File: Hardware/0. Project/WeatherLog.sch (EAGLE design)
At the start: 40 parts, among them IC2 TP4056, IC3 DS3231/SO, IC4 DW01A-G, U2 FS8205A, U3 ATMEGA328P-AU, U4 RT9193-33GB

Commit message: Working on 1.0 schematic
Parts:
- removed D3: SS16, diode:SUPPRESSOR-SMBJ
- removed LED1, LED2: (no value), led:LEDCHIPLED_0805
- removed LED3: IN-PI556FCH, LED RGB SMD:IN-PI556FCH
- removed R13: 150R (5%), rcl:R-EU_R0603
- removed R14, R17: 50R (5%), rcl:R-EU_R0603
- added C1, C2: 1uF, rcl:C-EUC0805
- added LED6: RGBLED5050, adafruit:RGBLED5050
- added Q1: BC817, transistor-npn:BC817-40LT1SMD
- added R1: 10k, rcl:R-EU_R0603
- added R12: NC, rcl:R-EU_R0603
- added R2: 20R, rcl:R-EU_R0603
- added R8, R9: 1k, rcl:R-EU_R0603
- added U1: ESP8266EX, ESP8266EX:ESP8266EX
- added U5: 25Q80ASSIG, 25Q80ASSIG:25Q80ASSIG
- R6: value 1k -> 100k
- R7: value 1k -> 200R
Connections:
- removed net +5V: U4.VOUT
- removed net BAT_CHARGING: IC2.!CHRG, LED1.C, U3.PD0
- removed net BAT_STANDBY: IC2.!STDBY, LED2.C, U3.PD1
- removed net N$26: LED3.AB3, R17.2
- removed net V_BAT: BT1.+, C5.1, IC2.BAT, R20.1, R4.1, U4.EN, U4.VIN
- removed net V_POWER_SUPPLY: C4.1, D3.A, IC2.CE, IC2.VCC4, J1.3, R18.1, R6.2, R7.2
- new net !BAT_CHARGING!: IC2.!CHRG, LED6.GREEN_C, U3.PD0
- new net !BAT_STANDBY!: IC2.!STDBY, LED6.BLUE_C, U3.PD1
- new net N$1: Q1.B, R1.1
- new net N$12: LED6.BLUE_A, R9.1
- new net N$13: R7.1, U5.SCLK
- new net N$15: U1.SDIO_DATA_0, U5.MOSI
- new net N$23: R7.2, U1.SDIO_CLK
- new net N$24: R12.1, U1.!EXT_RSTB
- new net N$25: R12.2, U1.XPD_DCDC
- new net N$3: LED6.RED_C, Q1.C
- new net N$5: LED6.RED_A, R2.1
- new net V_BAT+: BT1.+, C2.1, C5.1, IC2.BAT, R2.2, R20.1, R4.1, R6.2, U4.EN, U4.VIN
- new net V_BAT-: BT1.-, C3.2, IC4.GND, Q1.E, U2.S1_1
- new net V_EXTERNAL_SUPPLY: C1.1, C4.1, IC2.CE, IC2.VCC4, J1.3, R18.1, R8.2, R9.2, U4.VOUT
- net 3V: no longer D3.C
- net BAT_OVER_DISCHARGE_DETECTED: now also R1.2
- net GND: now also C1.2, C2.2, R6.1; no longer LED3.KB4, LED3.KG6, LED3.KR5
- net LED_BLUE: no longer R17.1
- net LED_GREEN: no longer R14.1
- net LED_RED: no longer R13.1
- net N$10: now also LED6.GREEN_A, R8.1; no longer BT1.-, C3.2, IC4.GND, U2.S1_1
- net N$11: now also U1.SDIO_DATA_3, U5.!WP!; no longer LED1.A, R6.1
- net N$14: now also U1.SDIO_DATA_2, U5.!HOLD!; no longer LED2.A, R7.1
- net N$2: now also U1.SDIO_CMD, U5.!CS!; no longer LED3.AR2, R13.2
- net N$21: now also U1.SDIO_DATA_1, U5.MISO; no longer LED3.AG1, R14.2
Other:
- note added: "BATTERY STATUS"
- note added: "RECHARGEABLE BATTERY"
- note removed: "(Over-Charge & Over-Discharge)"
- note removed: "(outdoor WeatherLog Mode)"
- note removed: "LI-PO BATTERY"
- note removed: "USER INTERFACE"
- moved on the sheet: BT1, C3, C4, C5, C9, IC2, IC3, IC4, J1, R10, R11, R3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

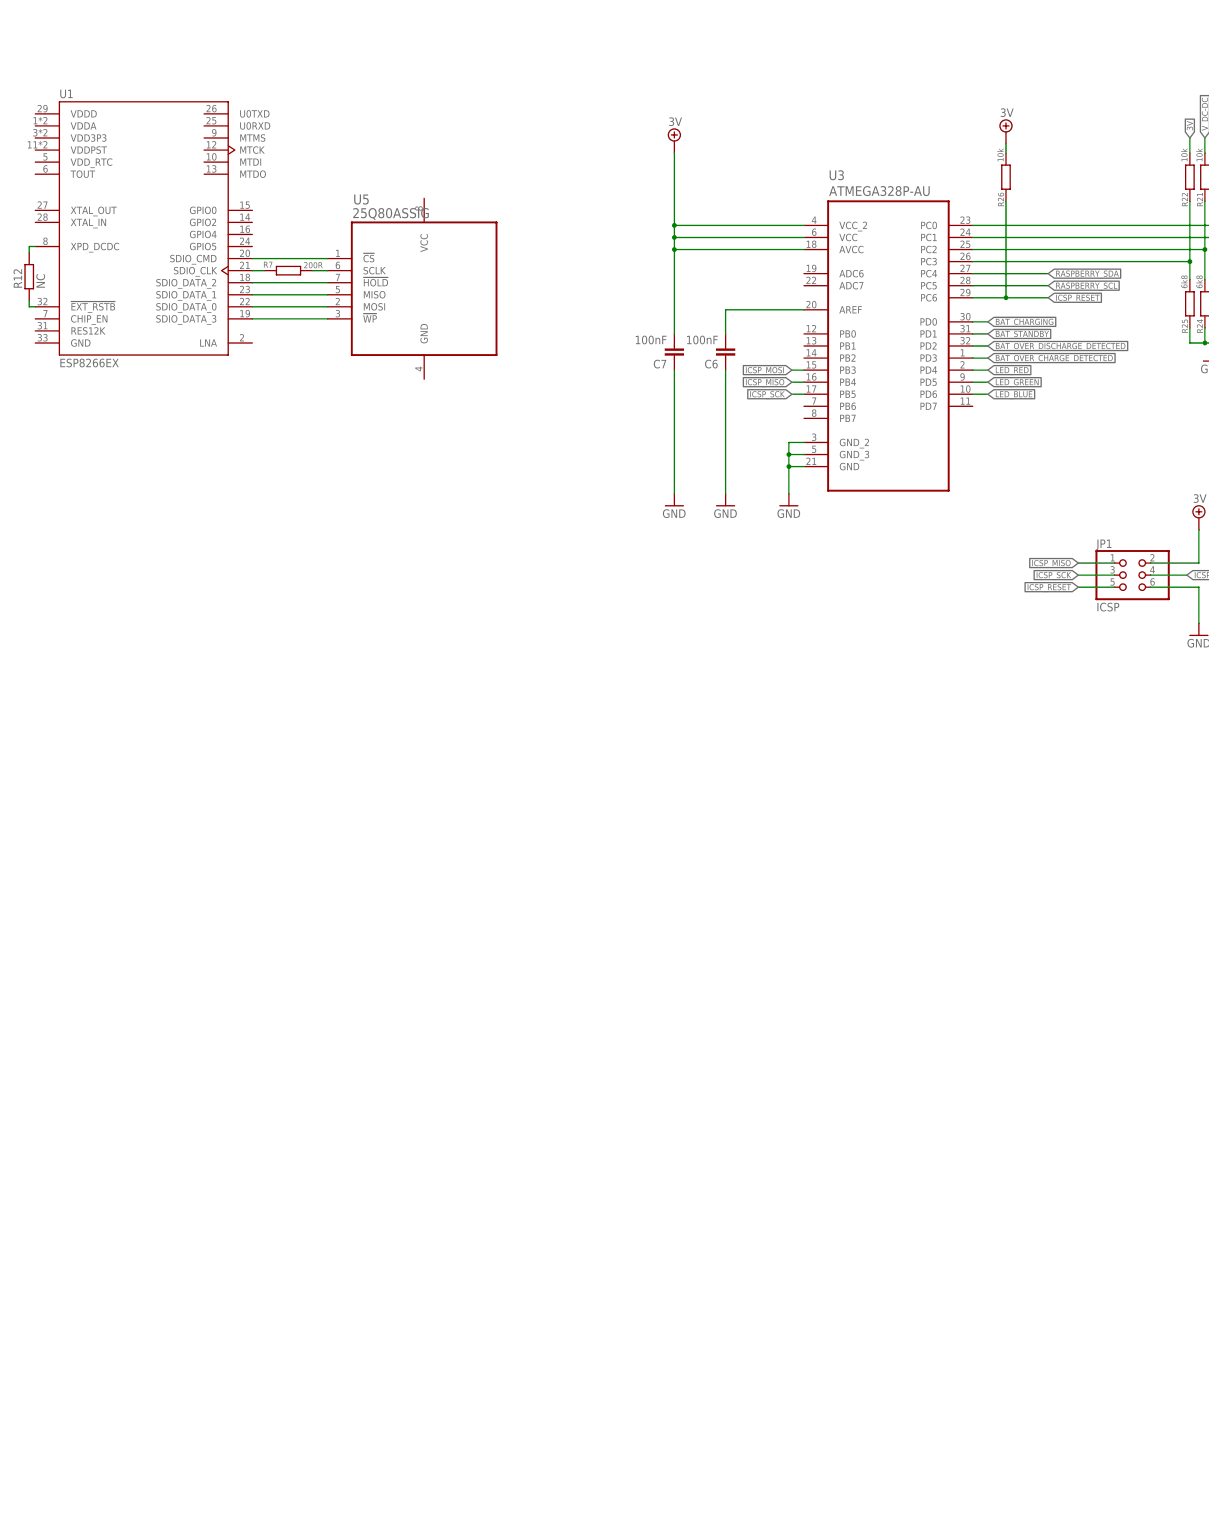
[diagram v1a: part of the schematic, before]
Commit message: Working on ESP8266EX circuit
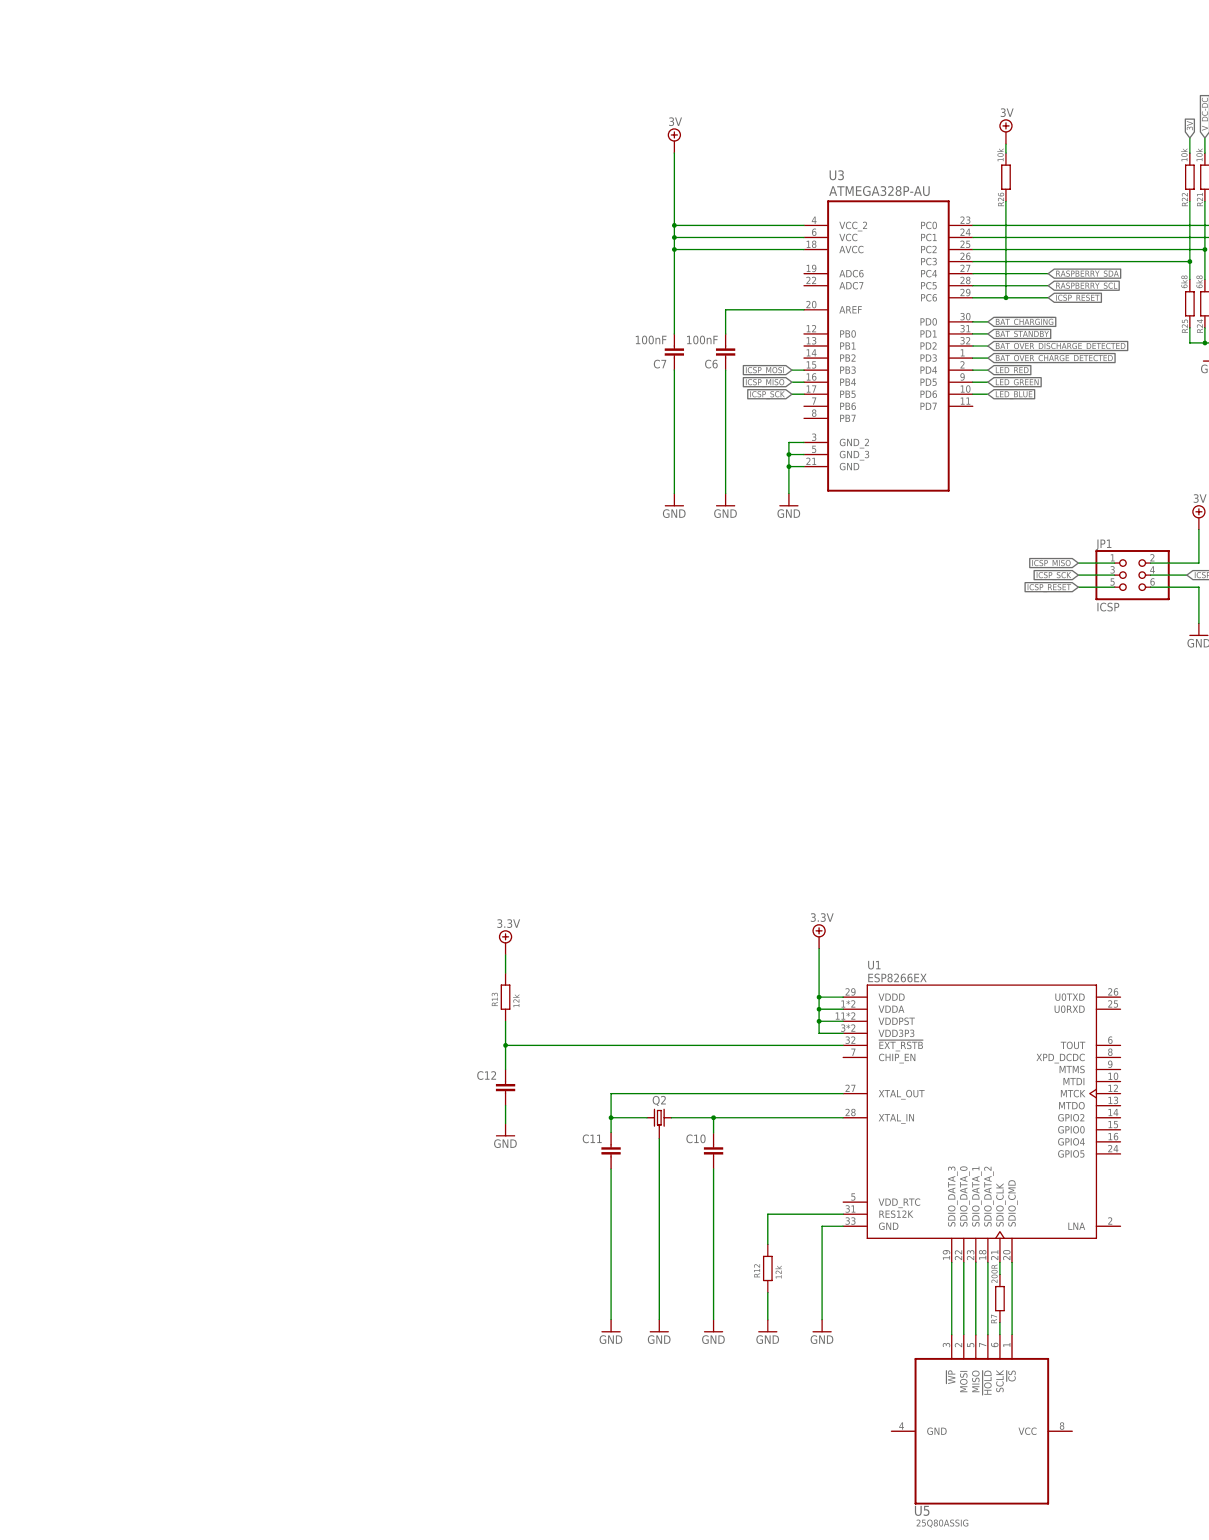
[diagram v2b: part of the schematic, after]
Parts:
- added C10, C11, C12: (no value), rcl:C-EUC0603
- added Q2: (no value), Crystal (SMD):KX-7
- added R13: 12k, rcl:R-EU_R0603
- R12: value NC -> 12k
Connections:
- new net +5V: R13.2, U1.VDD3P3, U1.VDDA, U1.VDDD, U1.VDDPST
- new net N$11: C11.2, Q2.1, U1.XTAL_OUT
- new net N$27: C10.2, Q2.2, U1.XTAL_IN
- net GND: now also C10.1, C11.1, C12.1, Q2.GND, R12.1, U1.GND
- net N$24: now also C12.2, R13.1; no longer R12.1
- net N$25: now also U1.RES12K; no longer U1.XPD_DCDC
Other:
- moved on the sheet: R12, R7, U1, U5

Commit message: All sensor circuits added
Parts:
- removed IC3: DS3231/SO, adafruit:DS3231/SO
- added A1: 50R IFA, PCB Antenna:ANTENNA
- added C13, C16: 100nF, rcl:C-EUC0603
- added C14: 2.4pF, rcl:C-EUC0603
- added C15: 3.0pF, rcl:C-EUC0603
- added C17: 1uF, rcl:C-EUC0603
- added C18: 10uF, rcl:C-EUC0603
- added C19: 1000uF x 10V, rcl:CPOL-EUE2-5
- added C20, C21, C22, C23, C24: 100nF, rcl:C-EUC0805
- added C25: 10uF, rcl:C-EUC0805
- added L1: 2.2 nH, rc-master-smd:L_0603
- added R14: 499R (1%), rcl:R-EU_R0603
- added R15, R27, R28, R29, R30, R31: 10k (5%), rcl:R-EU_R0603
- added R16, R17: 10k (5%), rcl:R-EU_M0805
- added R32: 270k (5%), rcl:R-EU_R0603
- added U10: VEML6070, VEML6070:VEML6070
- added U6: BMP280, BMP280:BMP280
- added U7: DS3231/SO, adafruit:DS3231/SO
- added U8: SI7021, SI7021:SI7021
- added U9: TSL2561FN, TSL2561:TSL2561FN
- C1: value 1uF -> 100nF; device rcl:C-EUC0805 -> rcl:C-EUC0603
- C10, C11: value (none) -> 6.8pF
- C12: value (none) -> 100nF
- Q2: value (none) -> 26MHz ±10ppm
- R12: value 12k -> 12k (1%)
- R13: value 12k -> 10k (5%)
- R26: value 10k -> 10k (5%)
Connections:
- net N$24 renamed !MCU_RESET!
- new net I2C_SCL: U10.SCL, U6.SCL/SCLK, U7.SCL, U8.SCL, U9.SCL
- new net I2C_SDA: U10.SDA, U6.SDA/MISO, U7.SDA, U8.SDA, U9.SDA
- new net MCU_ENABLE: C1.2, R15.1, U1.CHIP_EN
- new net MCU_PROG_MODE: R16.1, U1.GPIO0
- new net MCU_SCL: U1.GPIO5
- new net MCU_SDA: U1.(PWM3)GPIO4
- new net MCU_UART_RX: U1.U0RXD
- new net MCU_UART_TX: R14.2
- new net N$24: C15.2, L1.2, U1.LNA
- new net N$28: R14.1, U1.U0TXD
- new net N$29: A1.FEED, C14.2, L1.1
- new net N$30: R27.1, U7.!INT!/SQW
- new net N$31: R17.1, U1.(GPIO15/SPI_CS/U0RTS/PWM1)MTDO
- new net N$32: R28.1, U7.32KHZ
- new net N$33: R29.1, U9.INT
- new net N$34: R30.1, U6.MOSI
- new net N$35: R31.1, U10.ACK
- new net N$36: R32.1, U10.RST
- net +5V: now also C13.2, C16.2, C17.2, C18.2, C20.2, C21.2, C22.2, C23.2, C24.2, C25.2, C8.2, R15.2, R27.2, R28.2, R29.2, R30.2, R31.2, U10.VDD, U5.VCC, U6.VDD, U6.VDDIO, U7.VDD, U8.VDD, U9.VDD
- net 3V: no longer C8.2, IC3.VCC
- net GND: now also A1.GND, C1.1, C13.1, C14.1, C15.1, C16.1, C17.1, C18.1, C19.-, C20.1, C21.1, C22.1, C23.1, C24.1, C25.1, R16.2, R17.2, R32.2, U10.GND, U5.GND, U6.GND, U7.GND, U8.GND, U9.ADDR, U9.GND; no longer C1.2, IC3.GND, IC3.NC, IC3.NC1, IC3.NC2, IC3.NC3, IC3.NC4, IC3.NC5, IC3.NC6, IC3.NC7
- net N$13: now also U5.!CS!; no longer U5.SCLK
- net N$14: now also U1.SPI_CLK, U5.SCLK; no longer U1.SDIO_DATA_2, U5.!HOLD!
- net N$15: now also U1.SPI_HD, U5.!HOLD!; no longer U1.SDIO_DATA_0, U5.MOSI
- net N$2: now also R7.2, U1.SPI_CS0; no longer U1.SDIO_CMD, U5.!CS!
- net N$21: now also U1.SPI_MOSI; no longer U1.SDIO_DATA_1
- net N$23: now also U1.SPI_MISO, U5.MOSI; no longer R7.2, U1.SDIO_CLK
- net N$26: now also U1.SPI_WP; no longer U1.SDIO_DATA_3
- net N$9: now also U7.VBAT; no longer IC3.VBAT
- net RASPBERRY_SCL: no longer IC3.SCL
- net RASPBERRY_SDA: no longer IC3.SDA
- net V_EXTERNAL_SUPPLY: now also C19.+; no longer C1.1
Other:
- note added: "7-bits Slave Address 0b0101001 0x29"
- note added: "7-bits Slave Address 0b0111000 0x38"
- note added: "7-bits Slave Address 0b1000000 0x40"
- note added: "7-bits Slave Address 0b1101000 0x68"
- note added: "7-bits Slave Address 0b1110111 0x77"
- note added: "80 MHz harmonics suppressor"
- note added: "BAROMETRIC PRESSURE AND TEMPERATURE SENSOR"
- note added: "From ESP8266 Hardware Design Guidelines"
- note added: "HUMIDITY SENSOR"
- note added: "LUMINOSITY SENSOR"
- moved on the sheet: C1, C10, C11, C12, C8, G1, Q2, R12, R13, R7, U1, U5

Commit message: 1.0 schematic done
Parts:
- removed JP1: ICSP, pinhead:PINHD-2X3
- removed R22: 10k, rcl:R-EU_M0805
- removed R23, R24, R25: 6k8, rcl:R-EU_M0805
- removed R26: 10k (5%), rcl:R-EU_M0805
- added D4: BAT760, diode:DIODE-SOD323-W
- added LED2, LED3: (no value), led:LED3MM
- added Q3, Q4: BC817, transistor-npn:BC817-40LT1SMD
- added R33, R38, R39: 10k (5%), rcl:R-EU_R0603
- added R34, R35: 4k7 (5%), rcl:R-EU_R0603
- added R36: 1k (5%), rcl:R-EU_R0603
- added X3: USB Micro B, Micro USB Connector:ZX62D-B-5PA8
- C6, C7: device rcl:C-EUC0805 -> rcl:C-EUC0603
- R10: value 20k -> 10k
- R11: value 50k -> 5k
- R16: device rcl:R-EU_M0805 -> rcl:R-EU_R0603
- R18: value 10k -> 330k (5%); device rcl:R-EU_M0805 -> rcl:R-EU_R0603
- R19: value 6k8 -> 100k (5%); device rcl:R-EU_M0805 -> rcl:R-EU_R0603
- R20, R21: value 10k -> 270R; device rcl:R-EU_M0805 -> rcl:R-EU_0204/7
- R5: value 1k -> 1k2 (5%)
- U3: value ATMEGA328P-AU -> FT232RL; device Atmel_By_element14_Batch_1-00:ATMEGA328P-AU -> FT232RL:FT232RL
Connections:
- net MCU_ENABLE renamed ESP_ENABLE
- removed net !MCU_RESET!: C12.2, R13.1, U1.!EXT_RSTB
- removed net +5V: C13.2, C16.2, C17.2, C18.2, C20.2, C21.2, C22.2, C23.2, C24.2, C25.2, C8.2, R13.2, R15.2, R27.2, R28.2, R29.2, R30.2, R31.2, U1.VDD3P3, U1.VDDA, U1.VDDD, U1.VDDPST, U10.VDD, U5.VCC, U6.VDD, U6.VDDIO, U7.VDD, U8.VDD, U9.VDD
- removed net 3V: C7.2, JP1.2, R10.2, R22.1, R26.1, U3.AVCC, U3.VCC, U3.VCC_2
- removed net I2C_SCL: U10.SCL, U6.SCL/SCLK, U7.SCL, U8.SCL, U9.SCL
- removed net I2C_SDA: U10.SDA, U6.SDA/MISO, U7.SDA, U8.SDA, U9.SDA
- removed net ICSP_MISO: JP1.1, U3.PB4
- removed net ICSP_MOSI: JP1.4, U3.PB3
- removed net ICSP_RESET: JP1.5, R26.2, U3.PC6
- removed net ICSP_SCK: JP1.3, U3.PB5
- removed net LED_BLUE: U3.PD6
- removed net LED_GREEN: U3.PD5
- removed net LED_RED: U3.PD4
- removed net MCU_PROG_MODE: R16.1, U1.GPIO0
- removed net MCU_SCL: U1.GPIO5
- removed net MCU_SDA: U1.(PWM3)GPIO4
- removed net MCU_UART_RX: U1.U0RXD
- removed net MCU_UART_TX: R14.2
- removed net N$22: R18.2, R19.1, U3.PC0
- removed net RASPBERRY_SCL: U3.PC5
- removed net RASPBERRY_SDA: U3.PC4
- removed net V_DC-DC: R21.1
- new net !ESP_PROG_MODE!: Q4.C, R16.1, U1.GPIO0
- new net !ESP_RESET!: C12.2, Q3.C, R13.1, U1.!EXT_RSTB
- new net 3.3V: C13.2, C16.2, C17.2, C18.2, C19.+, C20.2, C21.2, C22.2, C23.2, C24.2, C25.2, C8.2, R13.2, R15.2, R16.2, R27.2, R28.2, R29.2, R30.2, R31.2, R33.2, R34.2, R35.2, U1.VDD3P3, U1.VDDA, U1.VDDD, U1.VDDPST, U10.VDD, U4.VOUT, U5.VCC, U6.VDD, U6.VDDIO, U7.VDD, U8.VDD, U9.VDD
- new net DTR: Q4.E, R38.2, U3.!DTR!
- new net ESP_I2C_SCL: R35.1, U1.GPIO5, U10.SCL, U6.SCL/SCLK, U7.SCL, U8.SCL, U9.SCL
- new net ESP_I2C_SDA: R34.1, U1.(PWM3)GPIO4, U10.SDA, U6.SDA/MISO, U7.SDA, U8.SDA, U9.SDA
- new net ESP_ICSP_UART_RX: U1.U0RXD, U3.TXD
- new net ESP_ICSP_UART_TX: R14.2, U3.RXD
- new net N$37: R33.1, U1.(U1TXD)GPIO2
- new net N$49: LED2.C, R20.2
- new net N$50: LED3.C, R21.2
- new net N$53: U3.USBDM, X3G$1.2
- new net N$54: U3.USBDP, X3G$1.3
- new net N$59: Q3.B, R38.1
- new net RTS: Q3.E, R39.1, U3.!RTS!
- new net VCC_IO: C6.2, LED2.A, LED3.A, U3.3V3OUT, U3.VCCIO
- new net VUSB1: C7.2, D4.A, X3G$1.1
- net !BAT_CHARGING!: no longer U3.PD0
- net !BAT_STANDBY!: no longer U3.PD1
- net BAT_OVER_CHARGE_DETECTED: no longer U3.PD3
- net BAT_OVER_DISCHARGE_DETECTED: no longer U3.PD2
- net GND: now also IC2.GND, R10.1, R19.1, U3.AGND, U3.GND1, U3.GND2, U3.GND3, U3.TEST, X3G$1.4, X3G$1.5; no longer IC2.GND_3, JP1.6, R16.2, R19.2, R23.2, R24.2, R25.2, U3.GND, U3.GND_2, U3.GND_3
- net N$16: now also R10.2, R36.1; no longer R10.1
- net N$17: now also R20.1, U3.CBUS0; no longer C6.2, U3.AREF
- net N$18: now also R18.1, R19.2, U1.TOUT; no longer R22.2, R25.1, U3.PC3
- net N$19: now also R21.1, U3.CBUS1; no longer R21.2, R24.1, U3.PC2
- net N$20: now also Q4.B, R39.2; no longer R20.2, R23.1, U3.PC1
- net V_BAT+: now also R18.2; no longer R20.1
- net V_EXTERNAL_SUPPLY: now also D4.C, IC2.VCC, R36.2, U3.VCC; no longer C19.+, IC2.VCC4, R18.1, U4.VOUT
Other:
- note added: "*"
- note added: "From TP4056 Datasheet"
- note added: "If TEMP pin’s voltage is below 45% or above 80% of supply voltage VCC for more than 0.15S, this means that battery’s temperature is too high or too low, charging is suspended."
- note added: "SoC MCU + Wi-Fi"
- note added: "USB TO SERIAL CONVERTER"
- note added: "UV SENSOR"
- note added: "VOLTAGE REGULATOR"
- note removed: "OUTDOOR MODE VOLTAGE REGULATOR"
- note removed: "POWER SUPPLY & BATTERY STATUS MONITOR"
- moved on the sheet: A1, BT1, C1, C10, C11, C12, C13, C14, C15, C16, C17, C18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
